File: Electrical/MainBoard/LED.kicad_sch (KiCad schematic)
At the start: 19 parts, among them U2 GSF7002DW, U3 GSF7002DW, U4 GSF7002DW, U8 GSF7002DW

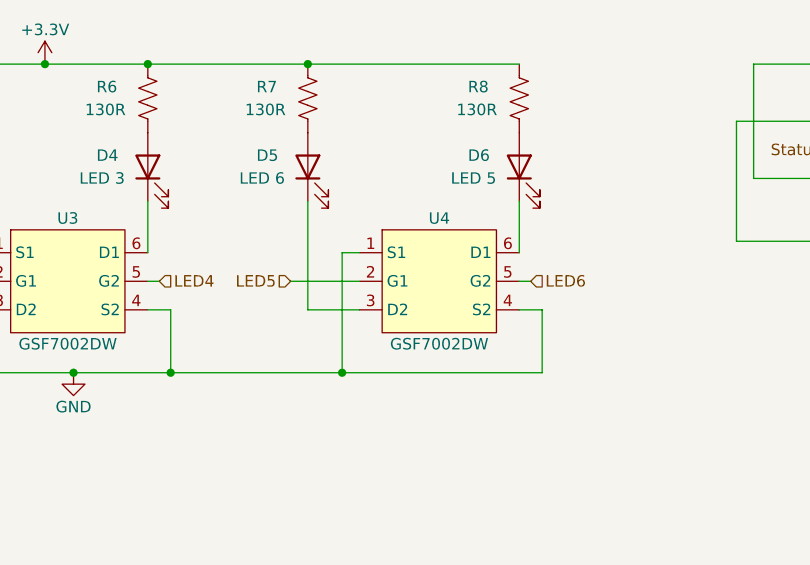
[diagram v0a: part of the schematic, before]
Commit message: Add more schematics and begin floorplanning
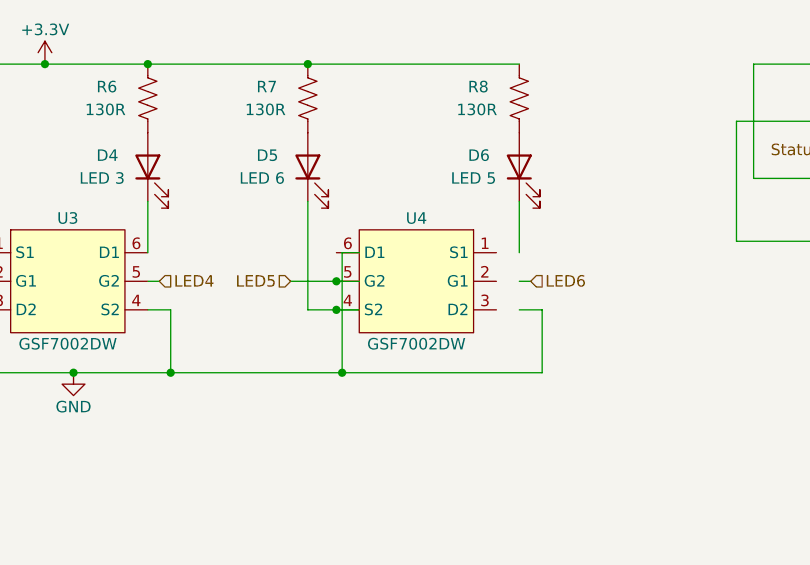
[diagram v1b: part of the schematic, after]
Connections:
- net GND: no longer U4.1 (S1), U4.4 (S2)
- net LED5: now also U4.5 (G2); no longer U4.2 (G1)
- net LED6: no longer U4.5 (G2)
- net at D5.1 (K): now also U4.4 (S2); no longer U4.3 (D2)
- net at U4.6 (D1): no longer D6.1 (K)
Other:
- moved on the sheet: U4
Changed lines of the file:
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@@
   (junction (at 168.275 73.025) (diameter 0) (color 0 0 0 0)
   )
+  (junction (at 189.23 100.33) (diameter 0) (color 0 0 0 0)
+  )
   (junction (at 156.845 73.025) (diameter 0) (color 0 0 0 0)
   )
+  (junction (at 189.23 97.155) (diameter 0) (color 0 0 0 0)
+  )
   (wire (pts (xy 127 93.98) (xy 127 88.265))
     (stroke (width 0) (type default))
@@
     (stroke (width 0) (type default))
   )
-  (wire (pts (xy 191.77 100.33) (xy 186.055 100.33))
+  (wire (pts (xy 191.77 100.33) (xy 189.23 100.33))
     (stroke (width 0) (type default))
   )
@@
     (stroke (width 0) (type default))
   )
+  (wire (pts (xy 189.23 97.155) (xy 191.77 97.155))
+    (stroke (width 0) (type default))
+  )
   (wire (pts (xy 271.78 92.71) (xy 264.795 92.71))
     (stroke (width 0) (type default))
@@
     (stroke (width 0) (type default))
   )
+  (wire (pts (xy 189.23 100.33) (xy 186.055 100.33))
+    (stroke (width 0) (type default))
+  )
   (wire (pts (xy 129.54 107.315) (xy 129.54 100.33))
     (stroke (width 0) (type default))
@@
     (stroke (width 0) (type default))
   )
-  (wire (pts (xy 184.15 97.155) (xy 191.77 97.155))
+  (wire (pts (xy 184.15 97.155) (xy 189.23 97.155))
     (stroke (width 0) (type default))
   )
@@
     )
   )
-  (symbol (lib_id "RobotLibary:GSF7002DW") (at 199.39 90.17 0) (unit 1)
-    (in_bom yes) (on_board yes) (dnp no)
-    (property "Reference" "U4" (at 200.66 90.17 0)
-      (effects (font (size 1.27 1.27)))
-    )
-    (property "Value" "GSF7002DW" (at 200.66 104.14 0)
-      (effects (font (size 1.27 1.27)))
-    )
+  (symbol (lib_id "RobotLibary:GSF7002DW") (at 199.39 90.17 0) (mirror y) (unit 1)
+    (in_bom yes) (on_board yes) (dnp no)
+    (property "Reference" "U4" (at 198.12 90.17 0)
+      (effects (font (size 1.27 1.27)))
+    )
+    (property "Value" "GSF7002DW" (at 198.12 104.14 0)
+      (effects (font (size 1.27 1.27)))
+    )

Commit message: Begin layout of pcb
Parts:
- renumbered D1 to D2, D2 to D3, D3 to D4, D4 to D5, D5 to D6, D6 to D7, R18 to R10, R17 to R11, R3 to R4, R4 to R5, R5 to R6, R6 to R7, R7 to R8, R8 to R9, U2 to U5, U3 to U6, U4 to U7
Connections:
- net GND: now also U7.1 (S1), U7.4 (S2)
- net LED5: now also U7.2 (G1); no longer U7.5 (G2)
- net LED6: now also U7.5 (G2)
- net at D6.1 (K): now also U7.3 (D2); no longer U7.4 (S2)
- net at U7.6 (D1): now also D7.1 (K)
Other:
- moved on the sheet: U7

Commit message: Add some finishing touches and create preliminary boms
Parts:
- D2: value LED 2 -> LED
- D3: value LED 1 -> LED
- D4: value LED 4 -> LED
- D5: value LED 3 -> LED
- D6: value LED 6 -> LED
- D7: value LED 5 -> LED
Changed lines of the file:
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@@
       (effects (font (size 1.27 1.27)) (justify right))
     )
-    (property "Value" "LED 2" (at 95.885 85.725 90)
+    (property "Value" "LED" (at 95.885 85.725 90)
       (effects (font (size 1.27 1.27)) (justify right))
     )
@@
       (effects (font (size 1.27 1.27)) (justify right))
     )
-    (property "Value" "LED 6" (at 178.435 85.725 90)
+    (property "Value" "LED" (at 178.435 85.725 90)
       (effects (font (size 1.27 1.27)) (justify right))
     )
@@
       (effects (font (size 1.27 1.27)) (justify right))
     )
-    (property "Value" "LED 4" (at 137.16 85.725 90)
+    (property "Value" "LED" (at 137.16 85.725 90)
       (effects (font (size 1.27 1.27)) (justify right))
     )
@@
       (effects (font (size 1.27 1.27)) (justify right))
     )
-    (property "Value" "LED 5" (at 201.93 85.725 90)
+    (property "Value" "LED" (at 201.93 85.725 90)
       (effects (font (size 1.27 1.27)) (justify right))
     )
@@
       (effects (font (size 1.27 1.27)) (justify right))
     )
-    (property "Value" "LED 1" (at 119.38 85.725 90)
+    (property "Value" "LED" (at 119.38 85.725 90)
       (effects (font (size 1.27 1.27)) (justify right))
     )
@@
       (effects (font (size 1.27 1.27)) (justify right))
     )
-    (property "Value" "LED 3" (at 160.655 85.725 90)
-      (effects (font (size 1.27 1.27)) (justify right))
-    )
+    (property "Value" "LED" (at 160.655 85.725 90)
+      (effects (font (size 1.27 1.27)) (justify right))
+    )

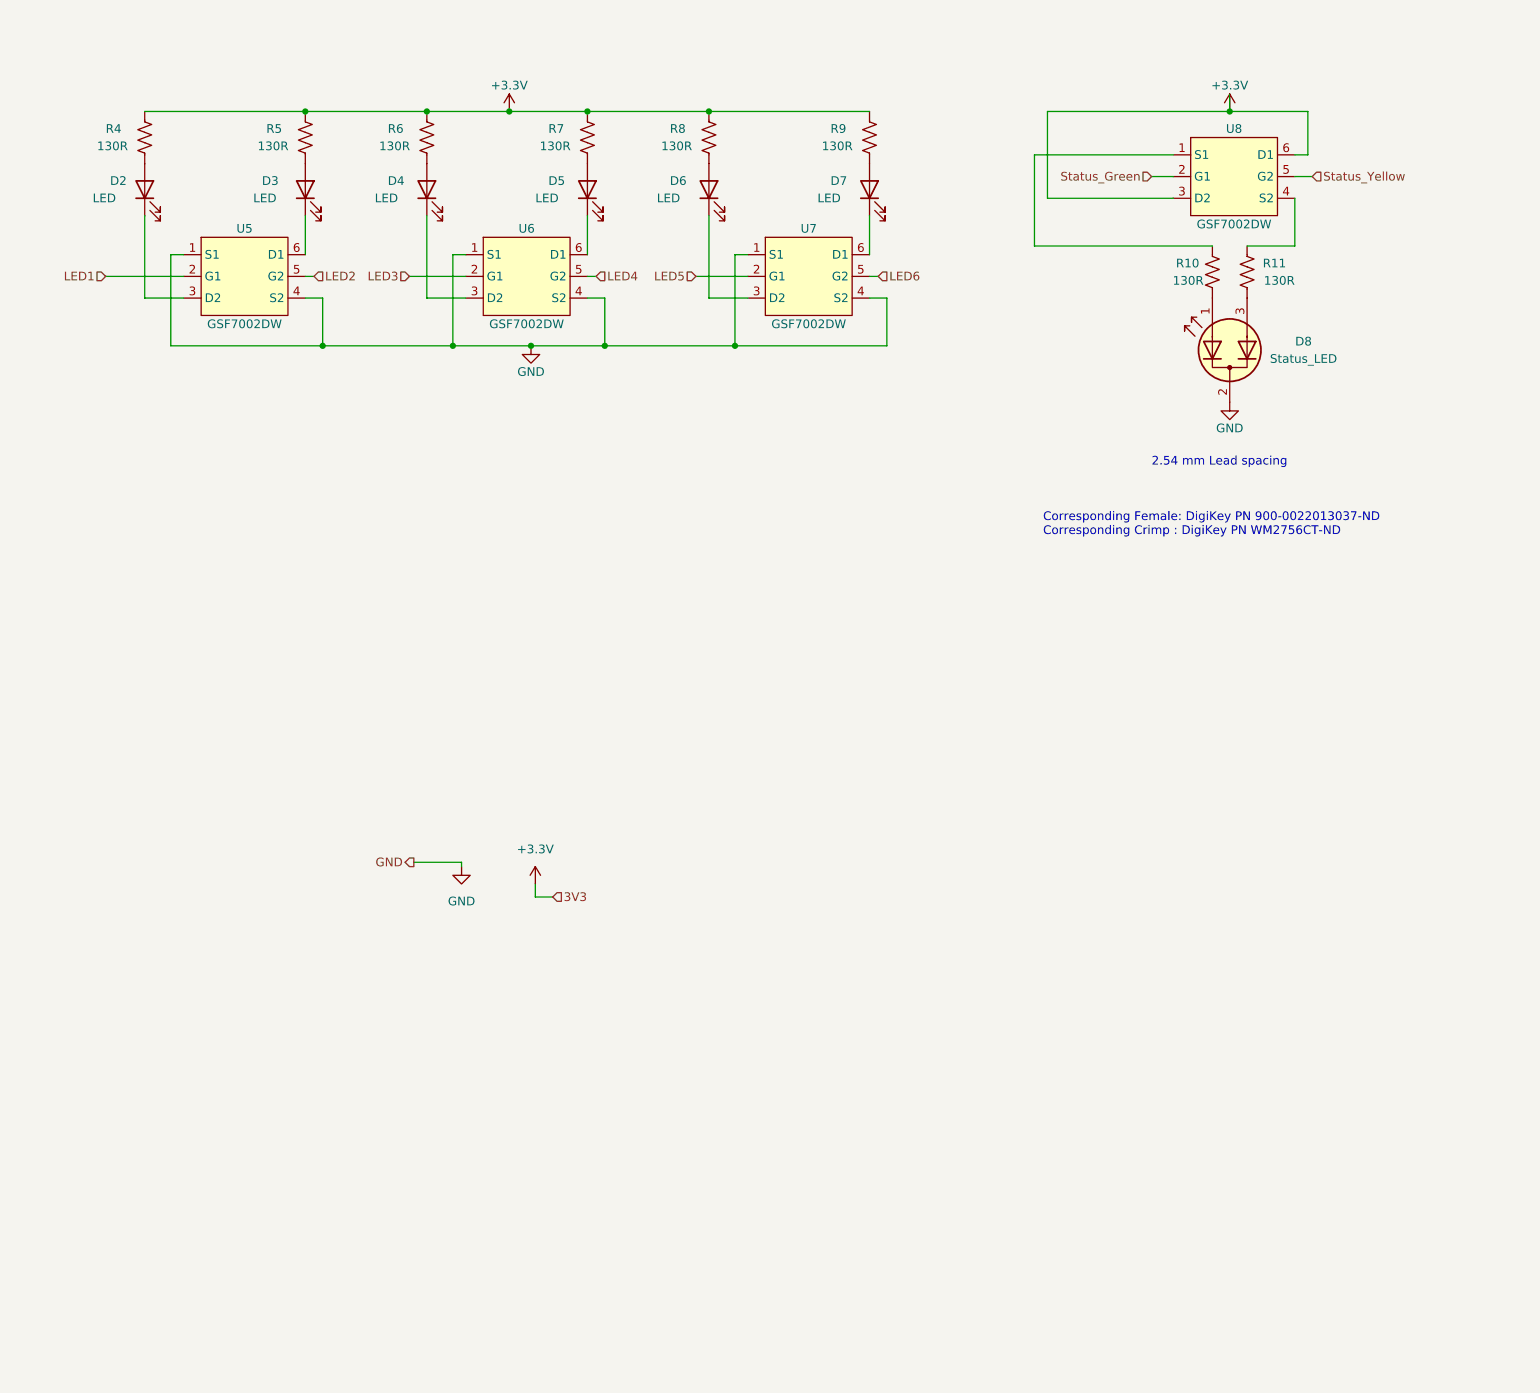
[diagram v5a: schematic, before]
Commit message: Fix SPI3 and make visual improvements
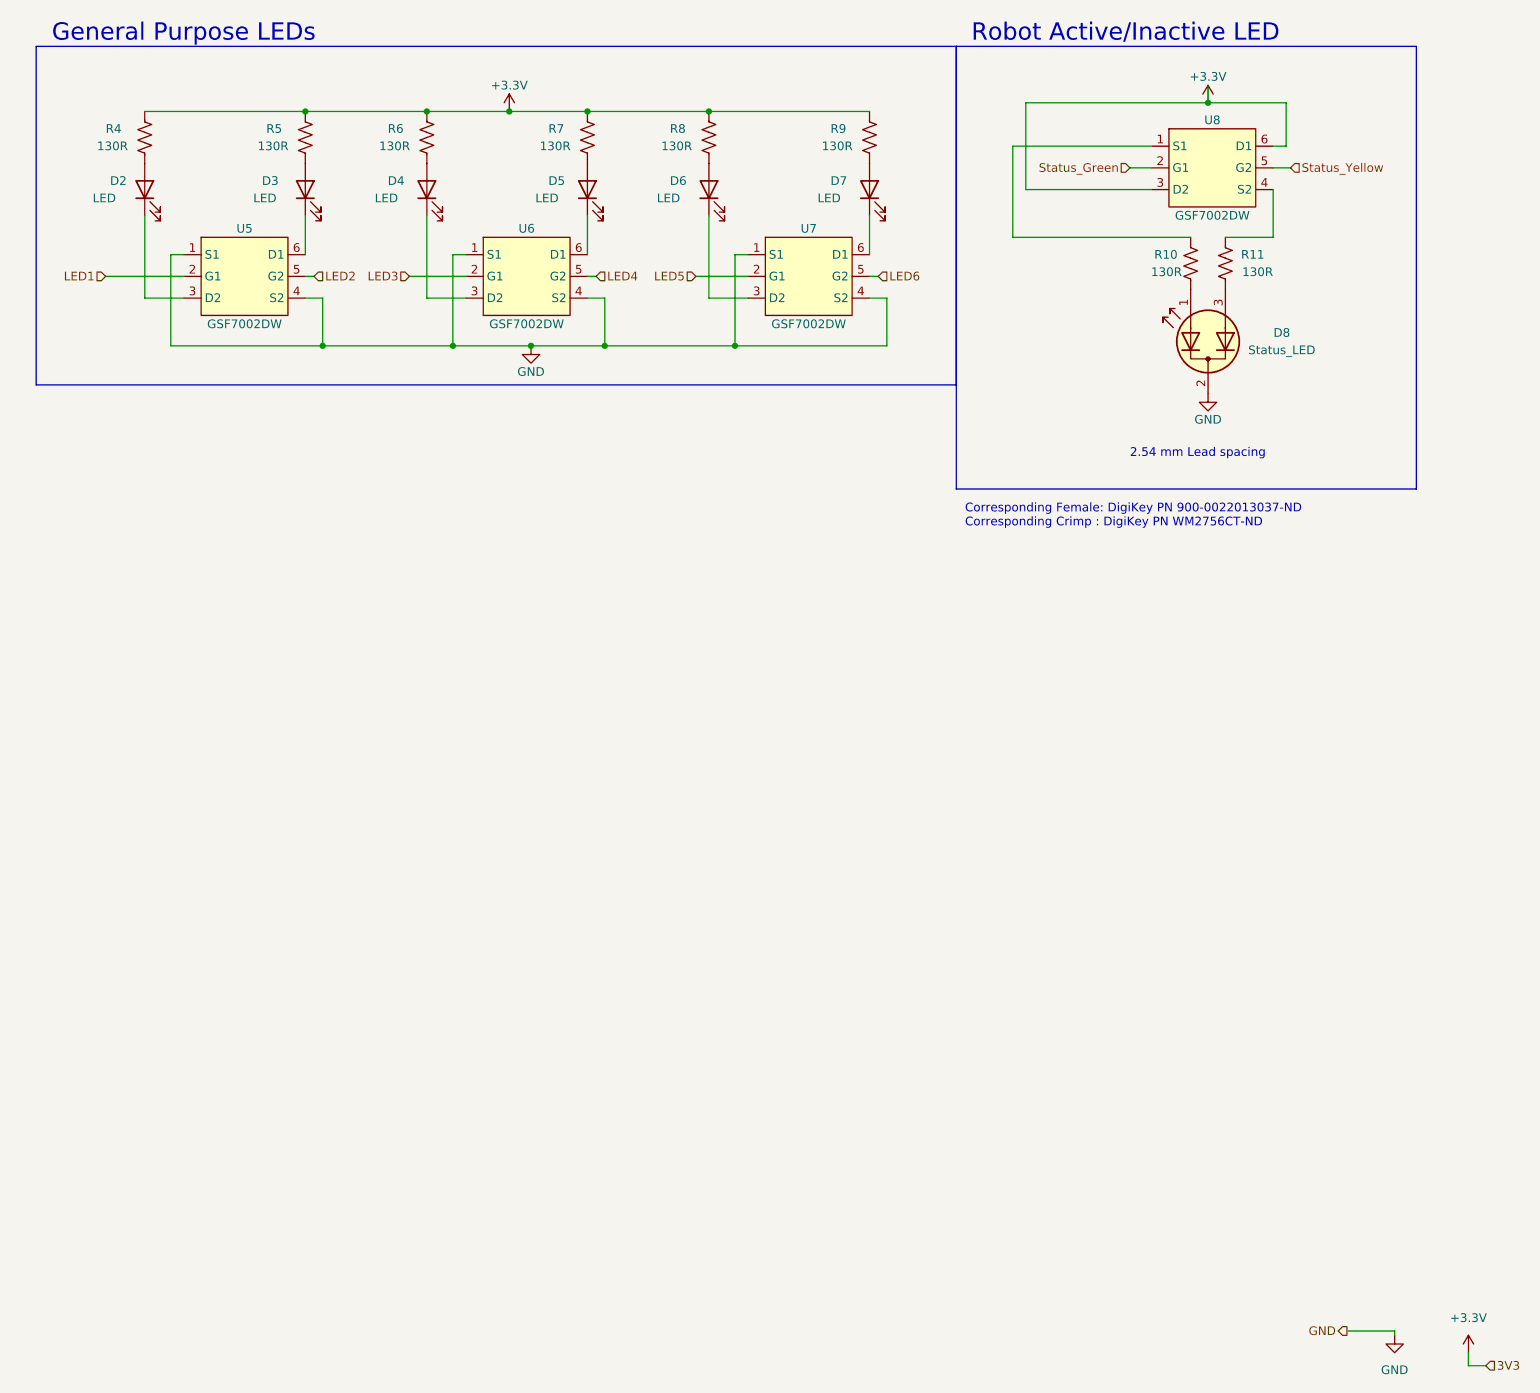
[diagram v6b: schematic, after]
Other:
- note added: "General Purpose LEDs"
- note added: "Robot Active/Inactive LED"
- moved on the sheet: D8, R10, R11, U8

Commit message: Add updated gerbers
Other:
- moved on the sheet: D2, D3, D4, D5, D6, D7, R4, R5, R6, R7, R8, R9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

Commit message: Update some parts
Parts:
- D2, D4, D6: Mfr Würth Elektronik -> Harvatek Corporation; Mfr P/N 150080RS75000 -> B1701URO-20D000114U1930; Supplier 1 P/N 732-4984-1-ND -> 3147-B1701URO-20D000114U1930CT-ND
- D3, D5, D7: Mfr Würth Elektronik -> Harvatek Corporation; Mfr P/N 150080VS75000 -> B1701UD--20D000414U1930; Supplier 1 P/N 732-4986-1-ND -> 3147-B1701UD--20D000414U1930CT-ND
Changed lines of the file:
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@@
 			)
 		)
-		(property "Datasheet" "https://www.we-online.com/katalog/datasheet/150080RS75000.pdf"
+		(property "Datasheet" "https://mm.digikey.com/Volume0/opasdata/d220001/medias/docus/3739/B1701URO-20D000114U1930.pdf"
 			(at 102.87 82.55 0)
 			(effects
@@
 			)
 		)
-		(property "Description" "LED RED CLEAR 0805 SMD"
+		(property "Description" "LED RED DIFFUSED 0805 SMD"
 			(at 102.87 82.55 0)
 			(effects
@@
 			)
 		)
-		(property "Mfr" "Würth Elektronik"
+		(property "Mfr" "Harvatek Corporation"
 			(at 102.87 82.55 0)
 			(effects
@@
 			)
 		)
-		(property "Mfr P/N" "150080RS75000"
+		(property "Mfr P/N" "B1701URO-20D000114U1930"
 			(at 102.87 82.55 0)
 			(effects
@@
 			)
 		)
-		(property "Supplier 1 P/N" "732-4984-1-ND"
+		(property "Supplier 1 P/N" "3147-B1701URO-20D000114U1930CT-ND"
 			(at 102.87 82.55 0)
 			(effects
@@
 			)
 		)
-		(property "Datasheet" "https://www.we-online.com/katalog/datasheet/150080RS75000.pdf"
+		(property "Datasheet" "https://mm.digikey.com/Volume0/opasdata/d220001/medias/docus/3739/B1701URO-20D000114U1930.pdf"
 			(at 185.42 82.55 0)
 			(effects
@@
 			)
 		)
-		(property "Description" "LED RED CLEAR 0805 SMD"
+		(property "Description" "LED RED DIFFUSED 0805 SMD"
 			(at 185.42 82.55 0)
 			(effects
@@
 			)
 		)
-		(property "Mfr" "Würth Elektronik"
+		(property "Mfr" "Harvatek Corporation"
 			(at 185.42 82.55 0)
 			(effects
@@
 			)
 		)
-		(property "Mfr P/N" "150080RS75000"
+		(property "Mfr P/N" "B1701URO-20D000114U1930"
 			(at 185.42 82.55 0)
 			(effects
@@
 			)
 		)
-		(property "Supplier 1 P/N" "732-4984-1-ND"
+		(property "Supplier 1 P/N" "3147-B1701URO-20D000114U1930CT-ND"
 			(at 185.42 82.55 0)
 			(effects
@@
 			)
 		)
-		(property "Datasheet" "https://www.we-online.com/katalog/datasheet/150080RS75000.pdf"
+		(property "Datasheet" "https://mm.digikey.com/Volume0/opasdata/d220001/medias/docus/3739/B1701URO-20D000114U1930.pdf"
 			(at 144.145 82.55 0)
 			(effects
@@
 			)
 		)
-		(property "Description" "LED RED CLEAR 0805 SMD"
+		(property "Description" "LED RED DIFFUSED 0805 SMD"
 			(at 144.145 82.55 0)
 			(effects
@@
 			)
 		)
-		(property "Mfr" "Würth Elektronik"
+		(property "Mfr" "Harvatek Corporation"
 			(at 144.145 82.55 0)
 			(effects
@@
 			)
 		)
-		(property "Mfr P/N" "150080RS75000"
+		(property "Mfr P/N" "B1701URO-20D000114U1930"
 			(at 144.145 82.55 0)
 			(effects
@@
 			)
 		)
-		(property "Supplier 1 P/N" "732-4984-1-ND"
+		(property "Supplier 1 P/N" "3147-B1701URO-20D000114U1930CT-ND"
 			(at 144.145 82.55 0)
 			(effects
@@
 			)
 		)
-		(property "Datasheet" "https://www.we-online.com/katalog/datasheet/150080RS75000.pdf"
+		(property "Datasheet" "https://mm.digikey.com/Volume0/opasdata/d220001/medias/docus/3656/B1701UD--20D000414U1930.pdf"
 			(at 208.915 82.55 0)
 			(effects
@@
 			)
 		)
-		(property "Description" "LED GREEN CLEAR 0805 SMD"
+		(property "Description" "LED ORANGE DIFFUSED 0805 SMD"
 			(at 208.915 82.55 0)
 			(effects
@@
 			)
 		)
-		(property "Mfr" "Würth Elektronik"
+		(property "Mfr" "Harvatek Corporation"
 			(at 208.915 82.55 0)
 			(effects
@@
 			)
 		)
-		(property "Mfr P/N" "150080VS75000"
+		(property "Mfr P/N" "B1701UD--20D000414U1930"
 			(at 208.915 82.55 0)
 			(effects
@@
 			)
 		)
-		(property "Supplier 1 P/N" "732-4986-1-ND"
+		(property "Supplier 1 P/N" "3147-B1701UD--20D000414U1930CT-ND"
 			(at 208.915 82.55 0)
 			(effects
@@
 			)
 		)
-		(property "Datasheet" "https://www.we-online.com/katalog/datasheet/150080RS75000.pdf"
+		(property "Datasheet" "https://mm.digikey.com/Volume0/opasdata/d220001/medias/docus/3656/B1701UD--20D000414U1930.pdf"
 			(at 126.365 82.55 0)
 			(effects
@@
 			)
 		)
-		(property "Description" "LED GREEN CLEAR 0805 SMD"
+		(property "Description" "LED ORANGE DIFFUSED 0805 SMD"
 			(at 126.365 82.55 0)
 			(effects
@@
 			)
 		)
-		(property "Mfr" "Würth Elektronik"
+		(property "Mfr" "Harvatek Corporation"
 			(at 126.365 82.55 0)
 			(effects
@@
 			)
 		)
-		(property "Mfr P/N" "150080VS75000"
+		(property "Mfr P/N" "B1701UD--20D000414U1930"
 			(at 126.365 82.55 0)
 			(effects
@@
 			)
 		)
-		(property "Supplier 1 P/N" "732-4986-1-ND"
+		(property "Supplier 1 P/N" "3147-B1701UD--20D000414U1930CT-ND"
 			(at 126.365 82.55 0)
 			(effects
@@
 			)
 		)
-		(property "Datasheet" "https://www.we-online.com/katalog/datasheet/150080RS75000.pdf"
+		(property "Datasheet" "https://mm.digikey.com/Volume0/opasdata/d220001/medias/docus/3656/B1701UD--20D000414U1930.pdf"
 			(at 167.64 82.55 0)
 			(effects
@@
 			)
 		)
-		(property "Description" "LED GREEN CLEAR 0805 SMD"
+		(property "Description" "LED ORANGE DIFFUSED 0805 SMD"
 			(at 167.64 82.55 0)
 			(effects
@@
 			)
 		)
-		(property "Mfr" "Würth Elektronik"
+		(property "Mfr" "Harvatek Corporation"
 			(at 167.64 82.55 0)
 			(effects
@@
 			)
 		)
-		(property "Mfr P/N" "150080VS75000"
+		(property "Mfr P/N" "B1701UD--20D000414U1930"
 			(at 167.64 82.55 0)
 			(effects
@@
 			)
 		)
-		(property "Supplier 1 P/N" "732-4986-1-ND"
+		(property "Supplier 1 P/N" "3147-B1701UD--20D000414U1930CT-ND"
 			(at 167.64 82.55 0)
 			(effects
